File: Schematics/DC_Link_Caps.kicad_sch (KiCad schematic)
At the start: 17 parts, among them J12 464379202, J13 464369202

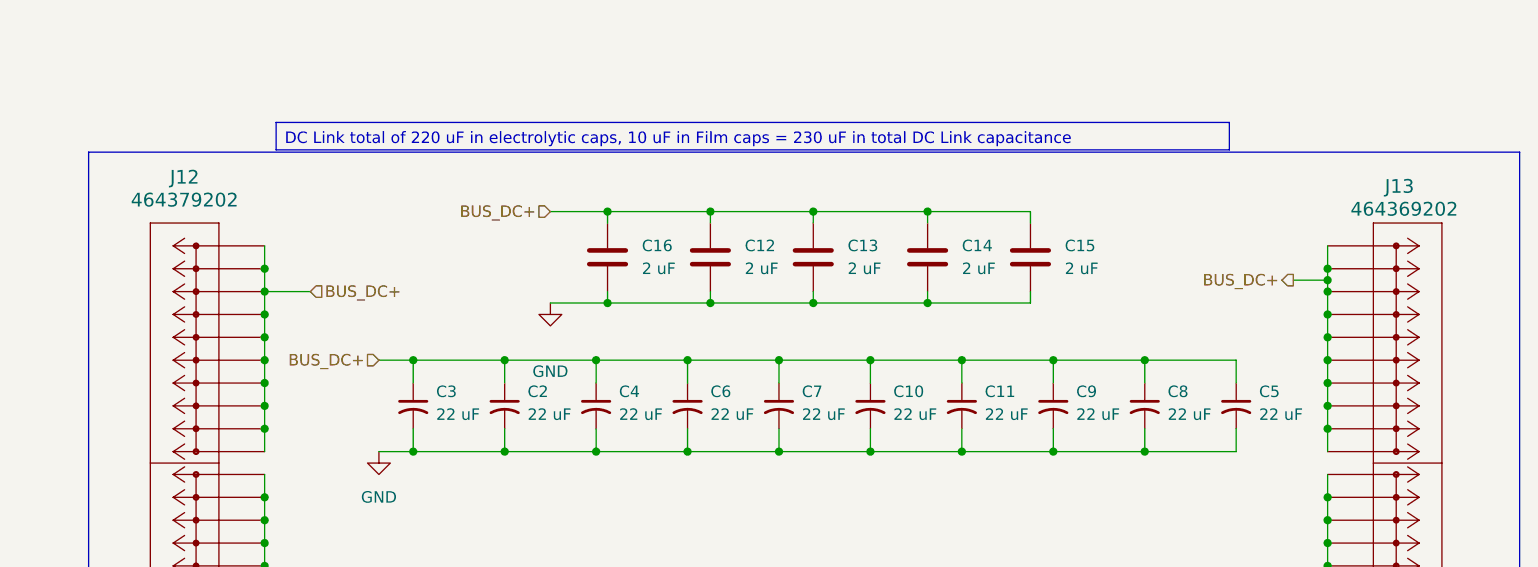
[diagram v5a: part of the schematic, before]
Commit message: [WIP Single Phase Inverter]
- Changed all Refs within each sub sheet (Stripe)
- Added 3V3 Power Supply off of 15V iso supply
- Added footprint, symbol and 3d part
- updated PCB with new part
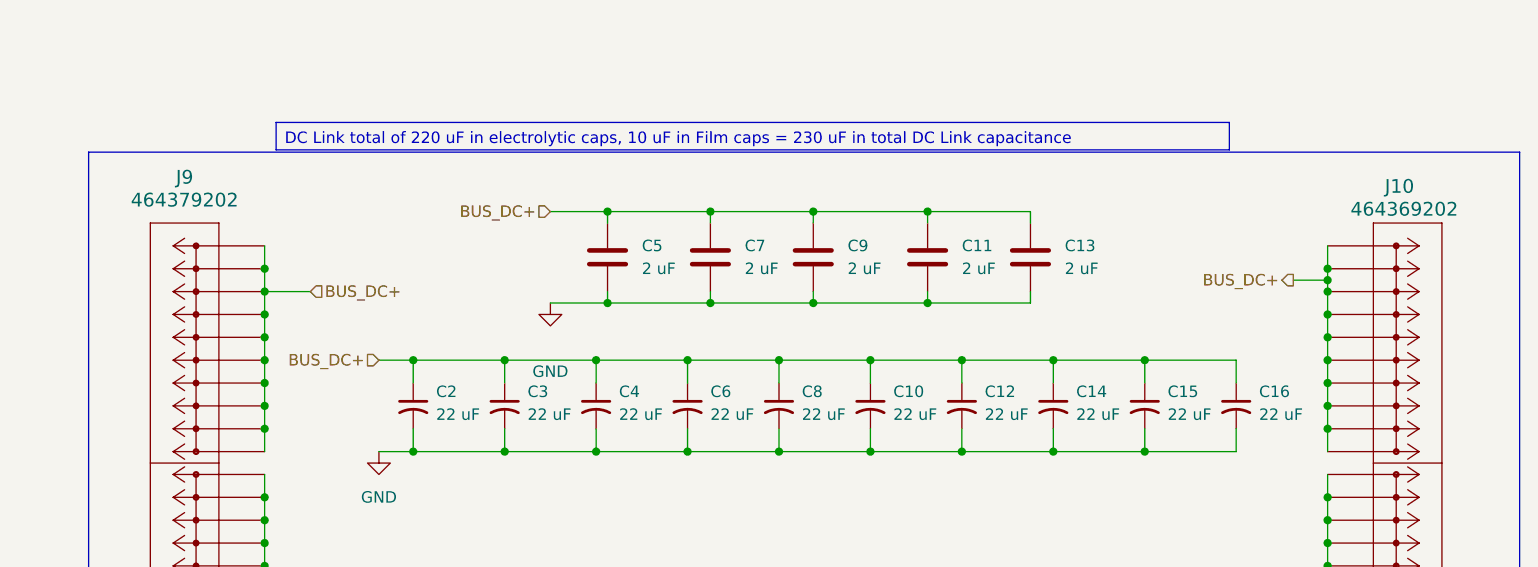
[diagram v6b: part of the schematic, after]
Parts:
- renumbered C14 to C11, C11 to C12, C15 to C13, C9 to C14, C8 to C15, C5 to C16, C3 to C2, C2 to C3, C16 to C5, C12 to C7, C7 to C8, C13 to C9, J13 to J10, J12 to J9
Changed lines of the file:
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@@
 		(dnp no)
 		(fields_autoplaced yes)
-		(property "Reference" "C15"
+		(property "Reference" "C13"
 			(at 222.25 80.0099 0)
 			(effects
@@
 			(project "SiC_Single_Phase_Inverter"
 				(path "/a1ed0539-9735-4ad1-a8fd-87e26e7fce16/9842b604-3f48-4932-a302-ed67fb523541"
-					(reference "C15")
+					(reference "C13")
 					(unit 1)
 				)
@@
 		(dnp no)
 		(fields_autoplaced yes)
-		(property "Reference" "#PWR090"
+		(property "Reference" "#PWR07"
 			(at 138.43 125.73 0)
 			(effects
@@
 			(project "SiC_Single_Phase_Inverter"
 				(path "/a1ed0539-9735-4ad1-a8fd-87e26e7fce16/9842b604-3f48-4932-a302-ed67fb523541"
-					(reference "#PWR090")
+					(reference "#PWR07")
 					(unit 1)
 				)
@@
 		(dnp no)
 		(fields_autoplaced yes)
-		(property "Reference" "C9"
+		(property "Reference" "C14"
 			(at 223.52 96.2151 0)
 			(effects
@@
 			(project "SiC_Single_Phase_Inverter"
 				(path "/a1ed0539-9735-4ad1-a8fd-87e26e7fce16/9842b604-3f48-4932-a302-ed67fb523541"
-					(reference "C9")
+					(reference "C14")
 					(unit 1)
 				)
@@
 		(dnp no)
 		(fields_autoplaced yes)
-		(property "Reference" "J12"
+		(property "Reference" "J9"
 			(at 124.46 72.39 0)
 			(effects
@@
 			(project "SiC_Single_Phase_Inverter"
 				(path "/a1ed0539-9735-4ad1-a8fd-87e26e7fce16/9842b604-3f48-4932-a302-ed67fb523541"
-					(reference "J12")
+					(reference "J9")
 					(unit 1)
 				)
@@
 		(dnp no)
 		(fields_autoplaced yes)
-		(property "Reference" "C12"
+		(property "Reference" "C7"
 			(at 186.69 80.0099 0)
 			(effects
@@
 			(project ""
 				(path "/a1ed0539-9735-4ad1-a8fd-87e26e7fce16/9842b604-3f48-4932-a302-ed67fb523541"
-					(reference "C12")
+					(reference "C7")
 					(unit 1)
 				)
@@
 		(dnp no)
 		(fields_autoplaced yes)
-		(property "Reference" "C16"
+		(property "Reference" "C5"
 			(at 175.26 80.0099 0)
 			(effects
@@
 			(project "SiC_Single_Phase_Inverter"
 				(path "/a1ed0539-9735-4ad1-a8fd-87e26e7fce16/9842b604-3f48-4932-a302-ed67fb523541"
-					(reference "C16")
+					(reference "C5")
 					(unit 1)
 				)
@@
 		(dnp no)
 		(fields_autoplaced yes)
-		(property "Reference" "C14"
+		(property "Reference" "C11"
 			(at 210.82 80.0099 0)
 			(effects
@@
 			(project "SiC_Single_Phase_Inverter"
 				(path "/a1ed0539-9735-4ad1-a8fd-87e26e7fce16/9842b604-3f48-4932-a302-ed67fb523541"
-					(reference "C14")
+					(reference "C11")
 					(unit 1)
 				)
@@
 		(on_board yes)
 		(dnp no)
-		(property "Reference" "J13"
+		(property "Reference" "J10"
 			(at 257.81 73.406 0)
 			(effects
@@
 			(project "SiC_Single_Phase_Inverter"
 				(path "/a1ed0539-9735-4ad1-a8fd-87e26e7fce16/9842b604-3f48-4932-a302-ed67fb523541"
-					(reference "J13")
+					(reference "J10")
 					(unit 1)
 				)
@@
 		(dnp no)
 		(fields_autoplaced yes)
-		(property "Reference" "C11"
+		(property "Reference" "C12"
 			(at 213.36 96.2151 0)
 			(effects
@@
 			(project "SiC_Single_Phase_Inverter"
 				(path "/a1ed0539-9735-4ad1-a8fd-87e26e7fce16/9842b604-3f48-4932-a302-ed67fb523541"
-					(reference "C11")
+					(reference "C12")
 					(unit 1)
 				)
@@
 		(dnp no)
 		(fields_autoplaced yes)
-		(property "Reference" "#PWR091"
+		(property "Reference" "#PWR010"
 			(at 246.38 127 0)
 			(effects
@@
 			(project "SiC_Single_Phase_Inverter"
 				(path "/a1ed0539-9735-4ad1-a8fd-87e26e7fce16/9842b604-3f48-4932-a302-ed67fb523541"
-					(reference "#PWR091")
+					(reference "#PWR010")
 					(unit 1)
 				)
@@
 		(dnp no)
 		(fields_autoplaced yes)
-		(property "Reference" "C7"
+		(property "Reference" "C8"
 			(at 193.04 96.2151 0)
 			(effects
@@
 			(project "SiC_Single_Phase_Inverter"
 				(path "/a1ed0539-9735-4ad1-a8fd-87e26e7fce16/9842b604-3f48-4932-a302-ed67fb523541"
-					(reference "C7")
+					(reference "C8")
 					(unit 1)
 				)
@@
 		(dnp no)
 		(fields_autoplaced yes)
-		(property "Reference" "C8"
+		(property "Reference" "C15"
 			(at 233.68 96.2151 0)
 			(effects
@@
 			(project "SiC_Single_Phase_Inverter"
 				(path "/a1ed0539-9735-4ad1-a8fd-87e26e7fce16/9842b604-3f48-4932-a302-ed67fb523541"
-					(reference "C8")
+					(reference "C15")
 					(unit 1)
 				)
@@
 		(dnp no)
 		(fields_autoplaced yes)
-		(property "Reference" "C13"
+		(property "Reference" "C9"
 			(at 198.12 80.0099 0)
 			(effects
@@
 			(project "SiC_Single_Phase_Inverter"
 				(path "/a1ed0539-9735-4ad1-a8fd-87e26e7fce16/9842b604-3f48-4932-a302-ed67fb523541"
-					(reference "C13")
+					(reference "C9")
 					(unit 1)
 				)
@@
 		(dnp no)
 		(fields_autoplaced yes)
-		(property "Reference" "C2"
+		(property "Reference" "C3"
 			(at 162.56 96.2151 0)
 			(effects
@@
 			(project ""
 				(path "/a1ed0539-9735-4ad1-a8fd-87e26e7fce16/9842b604-3f48-4932-a302-ed67fb523541"
-					(reference "C2")
+					(reference "C3")
 					(unit 1)
 				)
@@
 		(dnp no)
 		(fields_autoplaced yes)
-		(property "Reference" "C5"
+		(property "Reference" "C16"
 			(at 243.84 96.2151 0)
 			(effects
@@
 			(project "SiC_Single_Phase_Inverter"
 				(path "/a1ed0539-9735-4ad1-a8fd-87e26e7fce16/9842b604-3f48-4932-a302-ed67fb523541"
-					(reference "C5")
+					(reference "C16")
 					(unit 1)
 				)
@@
 		(dnp no)
 		(fields_autoplaced yes)
-		(property "Reference" "C3"
+		(property "Reference" "C2"
 			(at 152.4 96.2151 0)
 			(effects
@@
 			(project "SiC_Single_Phase_Inverter"
 				(path "/a1ed0539-9735-4ad1-a8fd-87e26e7fce16/9842b604-3f48-4932-a302-ed67fb523541"
-					(reference "C3")
-					(unit 1)
-				)
+					(reference "C2")
+					(unit 1)
+				)

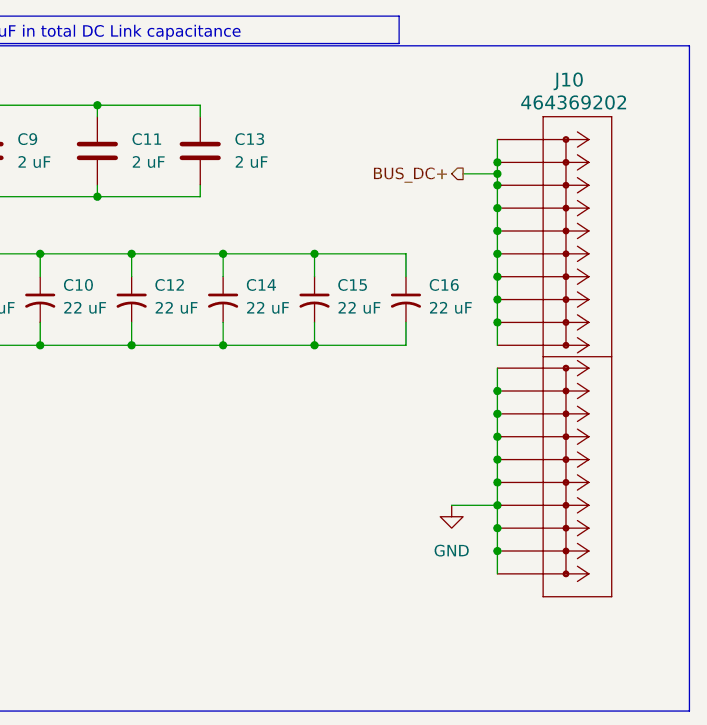
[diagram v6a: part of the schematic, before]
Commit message: [Milestone Compelted Controller and USB]
- Added Test Points
- Completed USB circuit to Controller
- Wired up Controller
- Added Connectors to Power Subsheet and 12pin from cotnroller to Full
  Bridge
- Added 3d models for USB compoents
- General fixes to subsheets
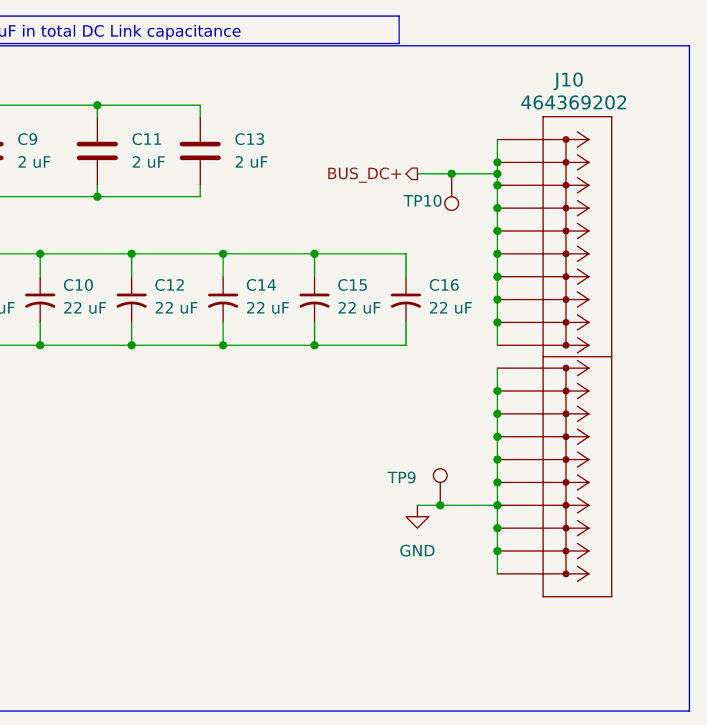
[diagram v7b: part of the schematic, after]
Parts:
- added TP10: 5277, SiC_Inverter:5277, symbol SiC_Inverter:5277
- added TP9: 5281, SiC_Inverter:5281, symbol SiC_Inverter:5281
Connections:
- net BUS_DC+: now also TP10.1
- net GND: now also TP9.1
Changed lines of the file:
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@@
+	)
+	(junction
+		(at 245.11 120.65)
+		(diameter 0)
+		(color 0 0 0 0)
 	)
 	(junction
@@
 	)
 	(junction
+		(at 246.38 83.82)
+		(diameter 0)
+		(color 0 0 0 0)
+	)
+	(junction
 		(at 133.35 87.63)
 		(diameter 0)
@@
 	(wire
 		(pts
+			(xy 246.38 83.82) (xy 251.46 83.82)
+		)
+		(stroke
+			(width 0)
+			(type default)
+		)
+	)
+	(wire
+		(pts
 			(xy 251.46 105.41) (xy 251.46 107.95)
 		)
@@
 	(wire
 		(pts
-			(xy 247.65 83.82) (xy 251.46 83.82)
+			(xy 242.57 83.82) (xy 246.38 83.82)
 		)
 		(stroke
@@
 	(wire
 		(pts
+			(xy 245.11 120.65) (xy 251.46 120.65)
+		)
+		(stroke
+			(width 0)
+			(type default)
+		)
+	)
+	(wire
+		(pts
 			(xy 251.46 110.49) (xy 251.46 113.03)
 		)
@@
 	(wire
 		(pts
-			(xy 246.38 120.65) (xy 251.46 120.65)
+			(xy 242.57 120.65) (xy 245.11 120.65)
 		)
 		(stroke
@@
 	(hierarchical_label "BUS_DC+"
 		(shape output)
-		(at 247.65 83.82 180)
+		(at 242.57 83.82 180)
 		(effects
 			(font
@@
 	)
 	(symbol
+		(lib_id "SiC_Inverter:5281")
+		(at 245.11 120.65 0)
+		(unit 1)
+		(exclude_from_sim no)
+		(in_bom yes)
+		(on_board yes)
+		(dnp no)
+		(property "Reference" "TP9"
+			(at 239.268 117.602 0)
+			(effects
+				(font
+					(size 1.27 1.27)
+				)
+				(justify left)
+			)
+		)
+		(property "Value" "5281"
+			(at 229.108 133.604 0)
+			(effects
+				(font
+					(size 1.27 1.27)
+				)
+				(hide yes)
+			)
+		)
+		(property "Footprint" "SiC_Inverter:5281"
+			(at 235.204 131.826 0)
+			(effects
+				(font
+					(size 1.27 1.27)
+				)
+				(hide yes)
+			)
+		)
+		(property "Datasheet" "https://www.keyelco.com/userAssets/file/K75p62.pdf"
+			(at 252.984 128.016 0)
+			(effects
+				(font
+					(size 1.27 1.27)
+				)
+				(hide yes)
+			)
+		)
+		(property "Description" "Test Plugs & Test Jacks TEST POINT BLACK MULTIPURPOSE"
+			(at 255.524 130.048 0)
+			(effects
+				(font
+					(size 1.27 1.27)
+				)
+				(hide yes)
+			)
+		)
+		(pin "1"
+		)
+		(instances
+			(project "SiC_Single_Phase_Inverter"
+				(path "/a1ed0539-9735-4ad1-a8fd-87e26e7fce16/9842b604-3f48-4932-a302-ed67fb523541"
+					(reference "TP9")
+					(unit 1)
+				)
+			)
+		)
+	)
+	(symbol
 		(lib_id "SiC_Inverter:MKP1848C52050JK2")
 		(at 218.44 81.28 0)
@@
 	)
 	(symbol
+		(lib_id "SiC_Inverter:5277")
+		(at 246.38 83.82 180)
+		(unit 1)
+		(exclude_from_sim no)
+		(in_bom yes)
+		(on_board yes)
+		(dnp no)
+		(property "Reference" "TP10"
+			(at 245.364 86.868 0)
+			(effects
+				(font
+					(size 1.27 1.27)
+				)
+				(justify left)
+			)
+		)
+		(property "Value" "5277"
+			(at 262.382 70.866 0)
+			(effects
+				(font
+					(size 1.27 1.27)
+				)
+				(hide yes)
+			)
+		)
+		(property "Footprint" "SiC_Inverter:5277"
+			(at 256.286 72.644 0)
+			(effects
+				(font
+					(size 1.27 1.27)
+				)
+				(hide yes)
+			)
+		)
+		(property "Datasheet" "https://www.keyelco.com/userAssets/file/K75p62.pdf"
+			(at 238.506 76.454 0)
+			(effects
+				(font
+					(size 1.27 1.27)
+				)
+				(hide yes)
+			)
+		)
+		(property "Description" "Test Plugs & Test Jacks TEST POINT (BLUE) - COMPACT"
+			(at 235.966 74.422 0)
+			(effects
+				(font
+					(size 1.27 1.27)
+				)
+				(hide yes)
+			)
+		)
+		(pin "1"
+		)
+		(instances
+			(project "SiC_Single_Phase_Inverter"
+				(path "/a1ed0539-9735-4ad1-a8fd-87e26e7fce16/9842b604-3f48-4932-a302-ed67fb523541"
+					(reference "TP10")
+					(unit 1)
+				)
+			)
+		)
+	)
+	(symbol
 		(lib_id "SiC_Inverter:MKP1848C52050JK2")
 		(at 207.01 81.28 0)
@@
 	(symbol
 		(lib_id "power:GND")
-		(at 246.38 120.65 0)
+		(at 242.57 120.65 0)
 		(unit 1)
 		(exclude_from_sim no)
@@
 		(fields_autoplaced yes)
 		(property "Reference" "#PWR010"
-			(at 246.38 127 0)
+			(at 242.57 127 0)
 			(effects
 				(font
@@
 		)
 		(property "Value" "GND"
-			(at 246.38 125.73 0)
+			(at 242.57 125.73 0)
 			(effects
 				(font
@@
 		)
 		(property "Footprint" ""
-			(at 246.38 120.65 0)
+			(at 242.57 120.65 0)
 			(effects
 				(font
@@
 		)
 		(property "Datasheet" ""
-			(at 246.38 120.65 0)
+			(at 242.57 120.65 0)
 			(effects
 				(font
@@
 		)
 		(property "Description" "Power symbol creates a global label with name \"GND\" , ground"
-			(at 246.38 120.65 0)
-			(effects
-				(font
+			(at 242.57 120.65 0)
+			(effects
+				(font

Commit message: WIP PCB, Added Test Points, added icon file
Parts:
- renumbered J9 to J10, J10 to J11, TP9 to TP10, TP10 to TP11
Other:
- moved on the sheet: TP11
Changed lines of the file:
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@@
 		(on_board yes)
 		(dnp no)
-		(property "Reference" "TP9"
+		(property "Reference" "TP10"
 			(at 239.268 117.602 0)
 			(effects
@@
 			(project "SiC_Single_Phase_Inverter"
 				(path "/a1ed0539-9735-4ad1-a8fd-87e26e7fce16/9842b604-3f48-4932-a302-ed67fb523541"
-					(reference "TP9")
+					(reference "TP10")
 					(unit 1)
 				)
@@
 		(dnp no)
 		(fields_autoplaced yes)
-		(property "Reference" "#PWR07"
+		(property "Reference" "#PWR08"
 			(at 138.43 125.73 0)
 			(effects
@@
 			(project "SiC_Single_Phase_Inverter"
 				(path "/a1ed0539-9735-4ad1-a8fd-87e26e7fce16/9842b604-3f48-4932-a302-ed67fb523541"
-					(reference "#PWR07")
+					(reference "#PWR08")
 					(unit 1)
 				)
@@
 		(on_board yes)
 		(dnp no)
-		(property "Reference" "#PWR09"
+		(property "Reference" "#PWR010"
 			(at 165.1 92.71 0)
 			(effects
@@
 			(project "SiC_Single_Phase_Inverter"
 				(path "/a1ed0539-9735-4ad1-a8fd-87e26e7fce16/9842b604-3f48-4932-a302-ed67fb523541"
-					(reference "#PWR09")
+					(reference "#PWR010")
 					(unit 1)
 				)
@@
 		(dnp no)
 		(fields_autoplaced yes)
-		(property "Reference" "J9"
+		(property "Reference" "J10"
 			(at 124.46 72.39 0)
 			(effects
@@
 			(project "SiC_Single_Phase_Inverter"
 				(path "/a1ed0539-9735-4ad1-a8fd-87e26e7fce16/9842b604-3f48-4932-a302-ed67fb523541"
-					(reference "J9")
+					(reference "J10")
 					(unit 1)
 				)
@@
 	(symbol
 		(lib_id "SiC_Inverter:5277")
-		(at 246.38 83.82 180)
-		(unit 1)
-		(exclude_from_sim no)
-		(in_bom yes)
-		(on_board yes)
-		(dnp no)
-		(property "Reference" "TP10"
-			(at 245.364 86.868 0)
+		(at 246.38 82.55 180)
+		(unit 1)
+		(exclude_from_sim no)
+		(in_bom yes)
+		(on_board yes)
+		(dnp no)
+		(property "Reference" "TP11"
+			(at 245.364 85.598 0)
 			(effects
 				(font
@@
 		)
 		(property "Value" "5277"
-			(at 262.382 70.866 0)
+			(at 262.382 69.596 0)
 			(effects
 				(font
@@
 		)
 		(property "Footprint" "SiC_Inverter:5277"
-			(at 256.286 72.644 0)
+			(at 256.286 71.374 0)
 			(effects
 				(font
@@
 		)
 		(property "Datasheet" "https://www.keyelco.com/userAssets/file/K75p62.pdf"
-			(at 238.506 76.454 0)
+			(at 238.506 75.184 0)
 			(effects
 				(font
@@
 		)
 		(property "Description" "Test Plugs & Test Jacks TEST POINT (BLUE) - COMPACT"
-			(at 235.966 74.422 0)
-			(effects
-				(font
-					(size 1.27 1.27)
-				)
-				(hide yes)
-			)
-		)
-		(pin "1"
-		)
-		(instances
-			(project "SiC_Single_Phase_Inverter"
-				(path "/a1ed0539-9735-4ad1-a8fd-87e26e7fce16/9842b604-3f48-4932-a302-ed67fb523541"
-					(reference "TP10")
+			(at 235.966 73.152 0)
+			(effects
+				(font
+					(size 1.27 1.27)
+				)
+				(hide yes)
+			)
+		)
+		(pin "1"
+		)
+		(instances
+			(project "SiC_Single_Phase_Inverter"
+				(path "/a1ed0539-9735-4ad1-a8fd-87e26e7fce16/9842b604-3f48-4932-a302-ed67fb523541"
+					(reference "TP11")
 					(unit 1)
 				)
@@
 		(on_board yes)
 		(dnp no)
-		(property "Reference" "J10"
+		(property "Reference" "J11"
 			(at 257.81 73.406 0)
 			(effects
@@
 			(project "SiC_Single_Phase_Inverter"
 				(path "/a1ed0539-9735-4ad1-a8fd-87e26e7fce16/9842b604-3f48-4932-a302-ed67fb523541"
-					(reference "J10")
+					(reference "J11")
 					(unit 1)
 				)
@@
 		(dnp no)
 		(fields_autoplaced yes)
-		(property "Reference" "#PWR010"
+		(property "Reference" "#PWR011"
 			(at 242.57 127 0)
 			(effects
@@
 			(project "SiC_Single_Phase_Inverter"
 				(path "/a1ed0539-9735-4ad1-a8fd-87e26e7fce16/9842b604-3f48-4932-a302-ed67fb523541"
-					(reference "#PWR010")
+					(reference "#PWR011")
 					(unit 1)
 				)
@@
 		(dnp no)
 		(fields_autoplaced yes)
-		(property "Reference" "#PWR08"
+		(property "Reference" "#PWR09"
 			(at 146.05 109.22 0)
 			(effects
@@
 			(project "SiC_Single_Phase_Inverter"
 				(path "/a1ed0539-9735-4ad1-a8fd-87e26e7fce16/9842b604-3f48-4932-a302-ed67fb523541"
-					(reference "#PWR08")
-					(unit 1)
-				)
+					(reference "#PWR09")
+					(unit 1)
+				)
